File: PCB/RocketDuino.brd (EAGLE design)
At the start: 73 x 41 mm, 42 parts, among them J1 FTDI, Y1 16MHZ

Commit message: Cleanups from Reddit post
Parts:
- added C11, C12: 0.1uF, SparkFun-Capacitors:1206
- R1, R3: value 100Ω -> 150Ω
- R2, R4: value 150Ω -> 220Ω
- moved LOGO1 33.0 mm to (51.5, 37.0)
- moved SERIAL1 3.61 mm to (33.0, 4.00)
- moved RESET 2.25 mm to (18.2, 32.8)
- moved C9 2.15 mm to (16.5, 26.2), turned to 90 degrees
- moved POWER 1.00 mm to (44.8, 3.50)
- moved R1 1.00 mm to (44.8, 9.50)
- moved INFO 0.50 mm to (21.0, 6.00)
- moved R4 0.50 mm to (21.0, 11.0)
- moved GPS 0.25 mm to (24.0, 6.00)
- moved R3 0.25 mm to (24.0, 11.0)
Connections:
- net 5V: now also C11.1, C12.1
- net GND: now also C11.2, C12.2
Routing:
- net 5V: track 169.4 -> 173.2 mm, vias 2 -> 3
- net RESET: track 39.9 -> 36.7 mm
- net TX2: track 31.9 -> 35.0 mm, vias 1 -> 0
- net TX1: track 14.9 -> 17.8 mm
- net GND: track 96.5 -> 94.3 mm, vias 19 -> 21
- net RX1: track 15.7 -> 17.9 mm
- net RX2: track 34.0 -> 35.0 mm, vias 1 -> 0
- net LED_13: track 14.3 -> 13.8 mm

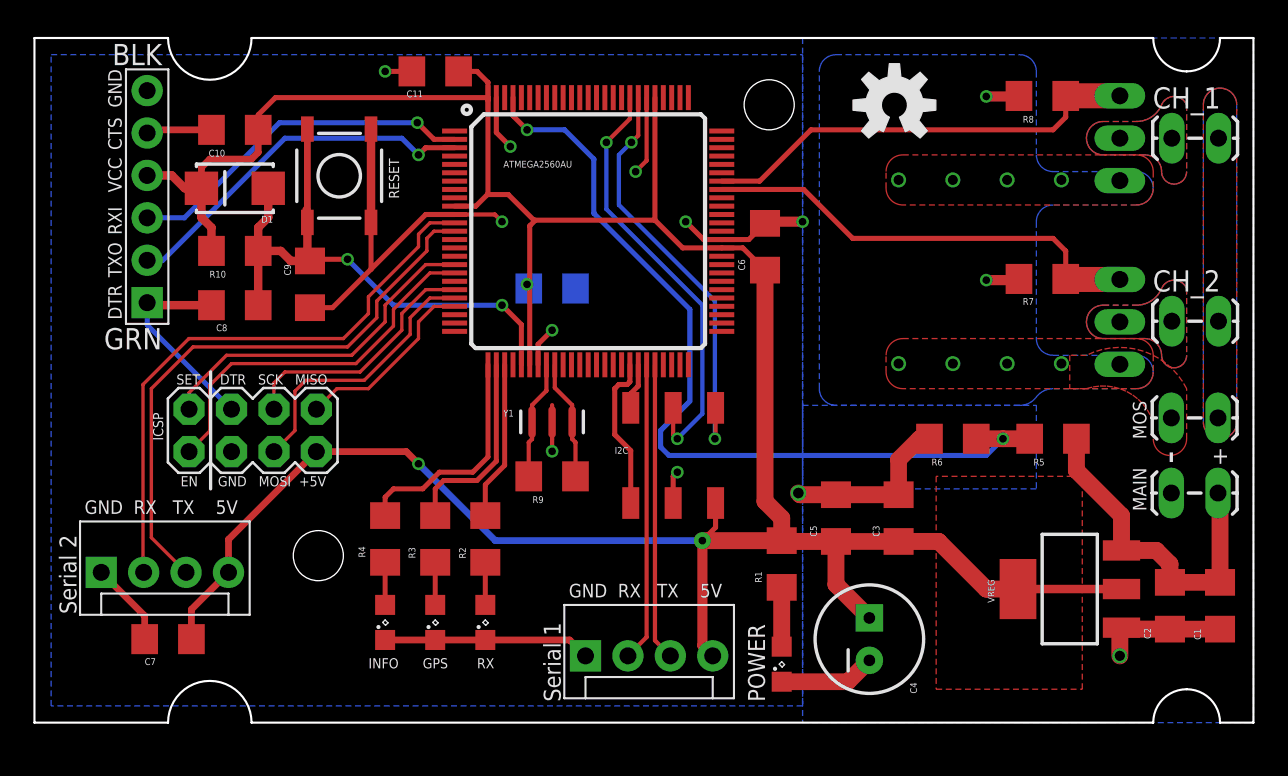
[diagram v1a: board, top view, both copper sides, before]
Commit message: Non-SMT I2C connector
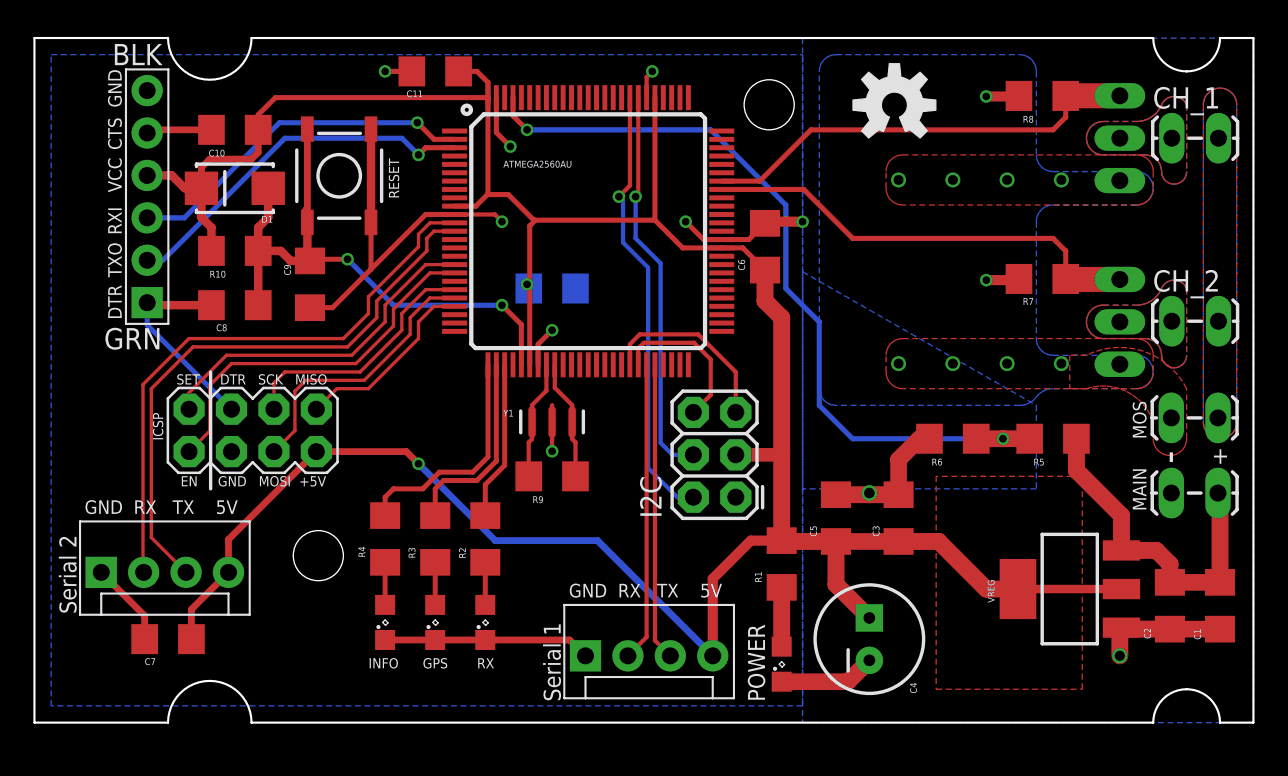
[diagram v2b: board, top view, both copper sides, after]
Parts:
- I2C: device SparkFun-Connectors:2X3_SMD -> SparkFun-Connectors:2X3
- moved I2C 4.51 mm to (42.0, 13.5), turned to 90 degrees
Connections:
- net 5V: now also I2C.3; no longer I2C.5
- net ADC14: now also I2C.2; no longer I2C.4
- net ADC15: now also I2C.4; no longer I2C.6
- net GND: now also I2C.1; no longer I2C.3
- net SCL: now also I2C.5; no longer I2C.1
- net SDA: now also I2C.6; no longer I2C.2
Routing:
- net GND: track 94.3 -> 87.2 mm, vias 21 -> 20
- net SDA: track 2.77 -> 9.48 mm
- net VSENSE: track 51.7 -> 47.5 mm
- net SCL: track 9.35 -> 11.2 mm
- net ADC15: track 25.2 -> 23.6 mm, vias 2 -> 1
- net 5V: track 173.2 -> 174.7 mm, vias 3 -> 2
- net ADC14: track 26.0 -> 26.6 mm, vias 2 -> 1

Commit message: Silkscreen Changes
Also re-routed the Vsense wire
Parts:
- moved LOGO1 51.2 mm to (4.00, 18.0)
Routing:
- net GND: track 87.2 -> 89.0 mm
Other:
- board text added: "RocketDuino"
- board text added: "V1.0"
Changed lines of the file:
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@@
 <wire x1="71" y1="41" x2="69" y2="39" width="0.127" layer="20" curve="-90"/>
 <wire x1="69" y1="39" x2="67" y2="41" width="0.127" layer="20" curve="-90"/>
-<text x="50" y="16" size="0.6096" layer="22" rot="MR0">vsense</text>
+<text x="52" y="17" size="0.6096" layer="22" rot="MR0">vsense</text>
 <text x="51.5" y="-8.25" size="1.778" layer="48">Joshua Villwock</text>
 <text x="70.5" y="15.5" size="1.016" layer="21">+</text>
@@
 <text x="1.5" y="11.25" size="1.016" layer="21" rot="R270">Serial 2</text>
 <text x="49" y="5.5" size="1.778" layer="22" rot="MR0">+</text>
+<text x="52" y="31" size="1.27" layer="21">RocketDuino</text>
+<text x="52" y="29" size="1.27" layer="21">V1.0</text>
 </plain>
 <attributes>
@@
 <element name="J1" library="SparkFun-Connectors" package="FTDI_DEVICE_SIDE" value="FTDI" x="6.75" y="31.5" locked="yes" rot="R90"/>
 <element name="D1" library="SparkFun-DiscreteSemi" package="SMA-DIODE_ALT" value="" x="12" y="32" rot="R180"/>
-<element name="LOGO1" library="SparkFun-Aesthetics" package="OSHW-LOGO-M" value="OSHW-LOGOM" x="51.5" y="36.98"/>
+<element name="LOGO1" library="SparkFun-Aesthetics" package="OSHW-LOGO-M" value="OSHW-LOGOM" x="4" y="17.98"/>
 <element name="INFO" library="led" package="SML0805" value="" x="21" y="6" smashed="yes" rot="R90">
 <attribute name="NAME" x="20" y="3.25" size="0.6096" layer="25"/>
@@
 <via x="61.5" y="32.5" extent="1-16" drill="0.6"/>
 <via x="37" y="39" extent="1-16" drill="0.4572"/>
-<via x="39" y="30" extent="1-16" drill="0.4572"/>
+<via x="38" y="31" extent="1-16" drill="0.4572"/>
 <wire x1="25.16" y1="30.43" x2="27.57" y2="30.43" width="0.254" layer="1"/>
 <wire x1="27.57" y1="30.43" x2="28" y2="30" width="0.254" layer="1"/>
@@
 <wire x1="41.16" y1="28.93" x2="42.78" y2="28.93" width="0.3048" layer="1"/>
 <wire x1="42.78" y1="28.93" x2="43.75" y2="29.9" width="0.3048" layer="1"/>
-<wire x1="41.16" y1="28.93" x2="40.07" y2="28.93" width="0.3048" layer="1"/>
-<wire x1="40.07" y1="28.93" x2="39" y2="30" width="0.3048" layer="1"/>
-<wire x1="30.16" y1="21.43" x2="30.16" y2="22.66" width="0.3" layer="1"/>
+<wire x1="41.16" y1="28.93" x2="39.32" y2="28.93" width="0.3048" layer="1"/>
 <wire x1="30.16" y1="22.66" x2="31" y2="23.5" width="0.3" layer="1"/>
 <via x="65" y="4" extent="1-16" drill="0.6096"/>
@@
 <wire x1="57" y1="26.5" x2="58.96" y2="26.5" width="0.6096" layer="1"/>
 <polygon width="0.254" layer="16" isolate="0.5" orphans="yes">
-<vertex x="46" y="27"/>
+<vertex x="46" y="39"/>
 <vertex x="60" y="19"/>
 <vertex x="60" y="14"/>
@@
 <wire x1="36.66" y1="38.66" x2="37" y2="39" width="0.254" layer="1"/>
 <contactref element="I2C" pad="1"/>
+<wire x1="30.16" y1="21.43" x2="30.16" y2="22.66" width="0.3" layer="1"/>
+<wire x1="39.32" y1="28.93" x2="38" y2="30.25" width="0.3048" layer="1"/>
+<wire x1="38" y1="30.25" x2="38" y2="31" width="0.3048" layer="1"/>
 </signal>
 <signal name="RESET">
@@
 <via x="58" y="17" extent="1-16" drill="0.4572"/>
 <wire x1="49" y1="17" x2="58" y2="17" width="0.3048" layer="16"/>
-<wire x1="47" y1="24" x2="47" y2="19" width="0.3048" layer="16"/>
-<wire x1="47" y1="19" x2="49" y2="17" width="0.3048" layer="16"/>
-<wire x1="29.5" y1="35.5" x2="40.5" y2="35.5" width="0.3048" layer="16"/>
-<wire x1="40.5" y1="35.5" x2="45" y2="31" width="0.3048" layer="16"/>
-<wire x1="45" y1="31" x2="45" y2="26" width="0.3048" layer="16"/>
-<wire x1="45" y1="26" x2="47" y2="24" width="0.3048" layer="16"/>
+<wire x1="44" y1="20" x2="46" y2="20" width="0.3048" layer="16"/>
+<wire x1="46" y1="20" x2="49" y2="17" width="0.3048" layer="16"/>
+<wire x1="39.5" y1="34" x2="39.5" y2="24.5" width="0.3048" layer="16"/>
+<wire x1="39.5" y1="24.5" x2="44" y2="20" width="0.3048" layer="16"/>
+<wire x1="29.5" y1="35.5" x2="38" y2="35.5" width="0.3048" layer="16"/>
+<wire x1="38" y1="35.5" x2="39.5" y2="34" width="0.3048" layer="16"/>
 </signal>
 <signal name="SCK">

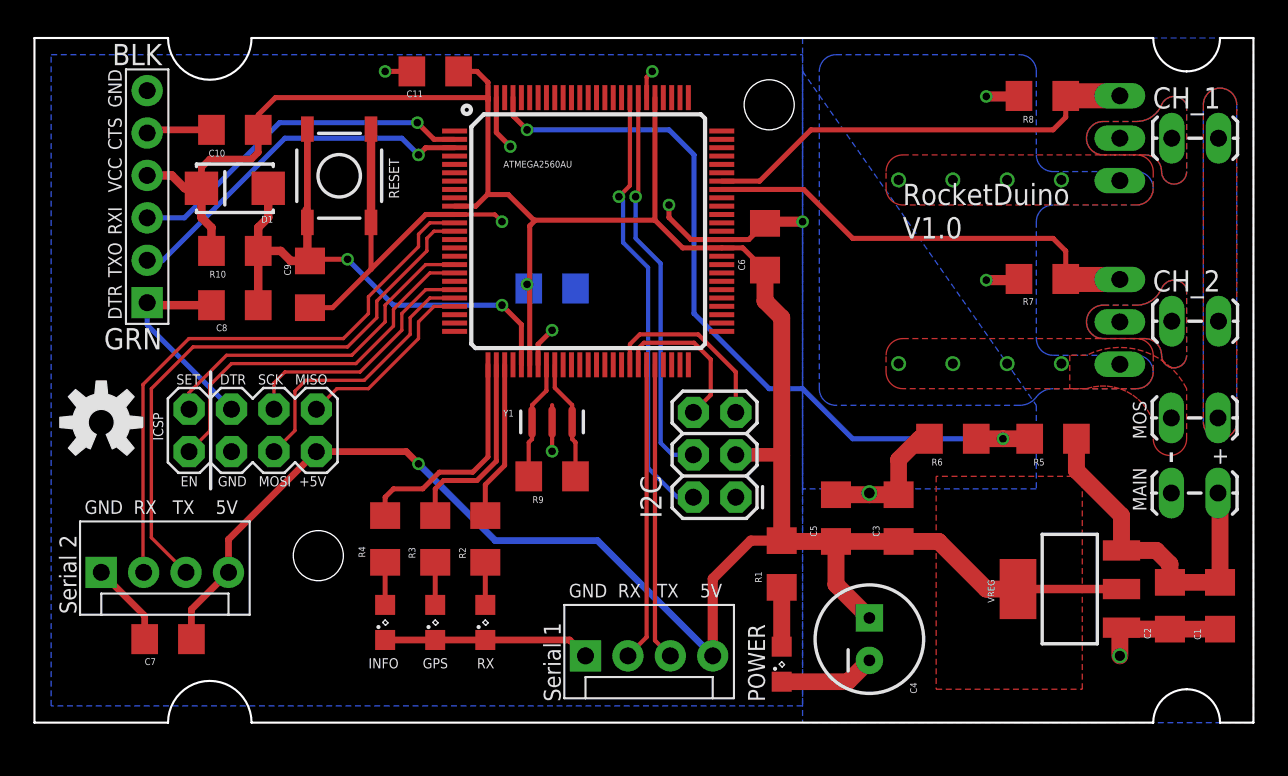
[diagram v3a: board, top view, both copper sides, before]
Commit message: Minor Re-routes of traces
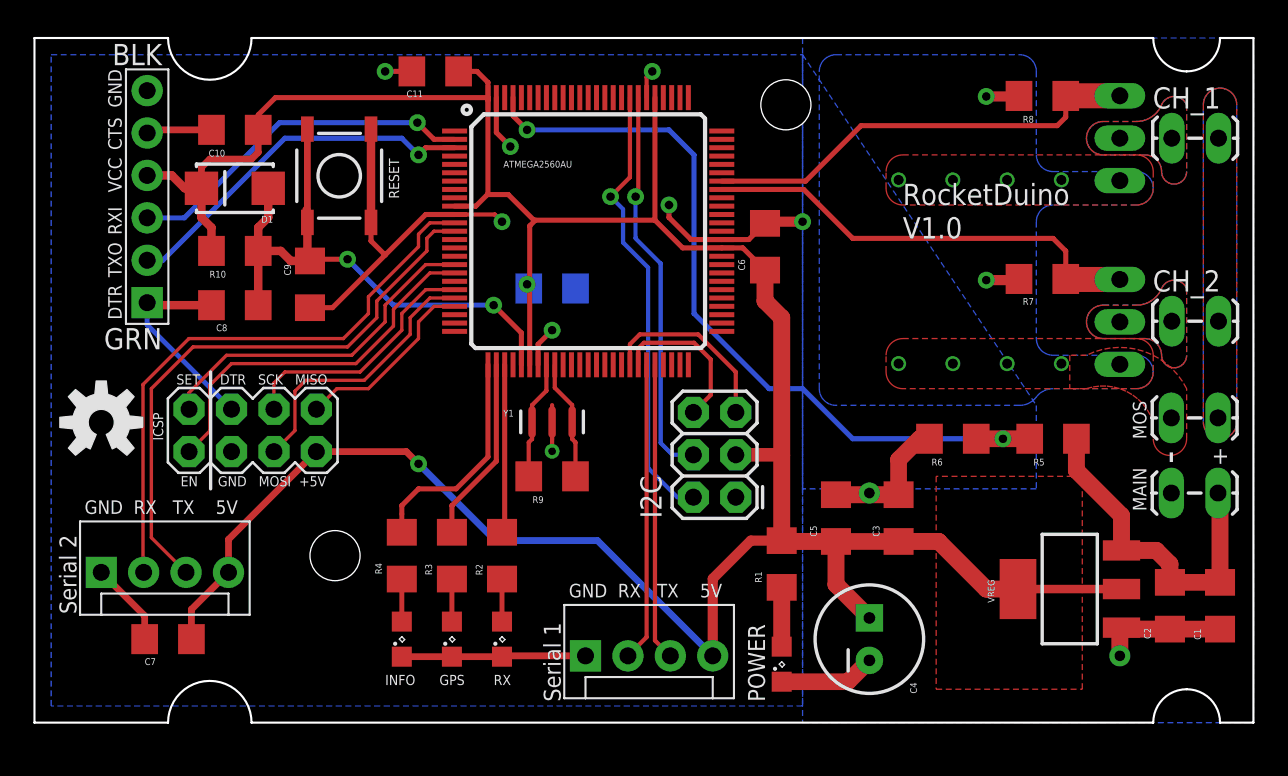
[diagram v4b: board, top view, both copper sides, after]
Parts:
- moved GPS 1.41 mm to (25.0, 5.00)
- moved INFO 1.41 mm to (22.0, 5.00)
- moved R2 1.41 mm to (28.0, 10.0)
- moved R3 1.41 mm to (25.0, 10.0)
- moved R4 1.41 mm to (22.0, 10.0)
- moved RX 1.41 mm to (28.0, 5.00)
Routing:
- net GND: track 89.0 -> 87.2 mm
- net LED_RX: track 9.51 -> 10.1 mm
- net LED_GPS: track 11.7 -> 11.1 mm

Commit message: Silkscreen changes
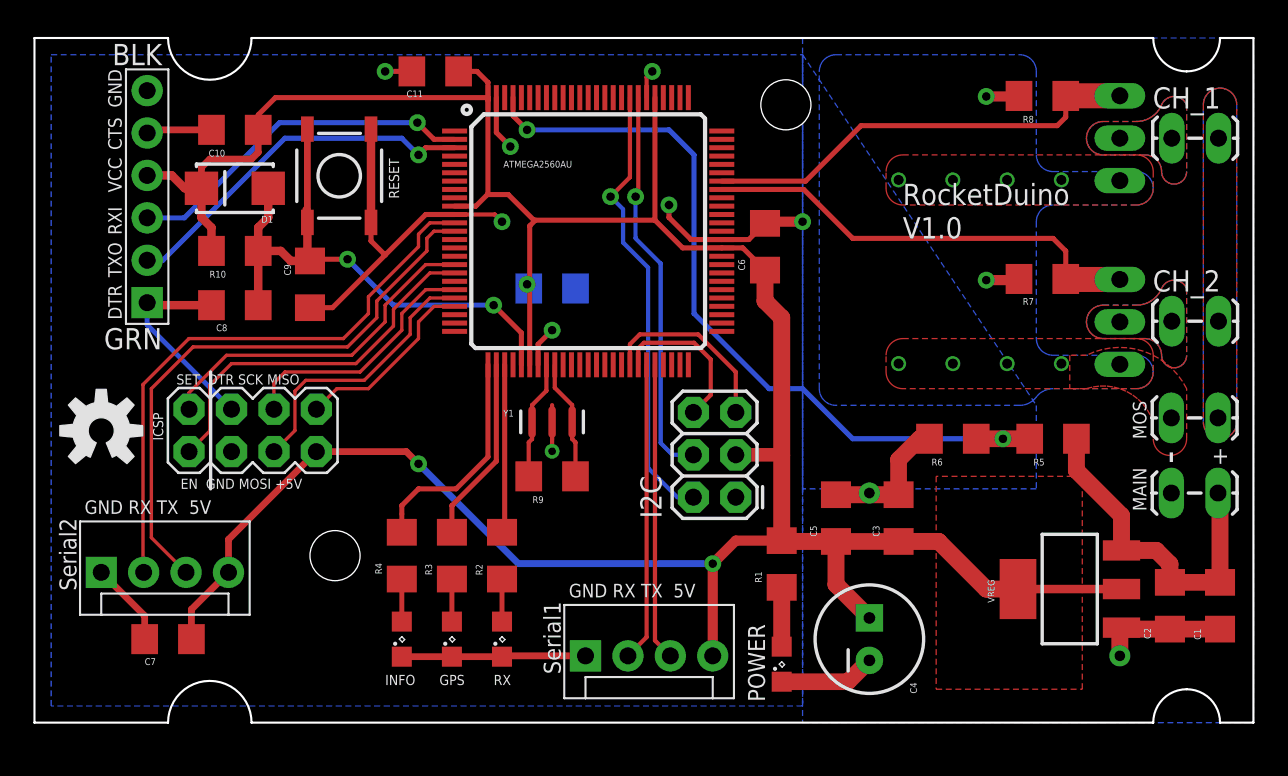
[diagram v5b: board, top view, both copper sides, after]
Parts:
- added LOGO2: OSHW-LOGOM, SparkFun-Aesthetics:OSHW-LOGO-M
- moved LOGO1 0.50 mm to (4.00, 17.5)
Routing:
- net 5V: track 174.7 -> 173.0 mm, vias 2 -> 3
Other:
- board text added: "Serial1"
- board text added: "Serial2"
- board text removed: "Serial 1"
- board text removed: "Serial 2"
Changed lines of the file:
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@@
 <setting verticaltext="up"/>
 </settings>
-<grid distance="39.3700787" unitdist="mil" unit="mil" style="lines" multiple="1" display="yes" altdistance="0.25" altunitdist="mm" altunit="mm"/>
+<grid distance="0.999999999" unitdist="mm" unit="mm" style="lines" multiple="1" display="yes" altdistance="0.25" altunitdist="mm" altunit="mm"/>
 <layers>
 <layer number="1" name="Top" color="4" fill="1" visible="yes" active="yes"/>
@@
 <wire x1="71" y1="41" x2="69" y2="39" width="0.127" layer="20" curve="-90"/>
 <wire x1="69" y1="39" x2="67" y2="41" width="0.127" layer="20" curve="-90"/>
-<text x="52" y="17" size="0.6096" layer="22" rot="MR0">vsense</text>
+<text x="37" y="35.75" size="0.6096" layer="22" rot="MR0">vsense</text>
 <text x="51.5" y="-8.25" size="1.778" layer="48">Joshua Villwock</text>
 <text x="70.5" y="15.5" size="1.016" layer="21">+</text>
@@
 <hole x="45" y="37" drill="3"/>
 <hole x="18" y="10" drill="3"/>
-<text x="8.5" y="20.25" size="0.6096" layer="21">SET     DTR   SCK   MISO</text>
-<text x="8.75" y="14.15" size="0.6096" layer="21">EN     GND   MOSI  +5V</text>
+<text x="8.5" y="20.25" size="0.6096" layer="21" font="vector" ratio="18">SET  DTR SCK MISO</text>
 <wire x1="10.55" y1="21" x2="10.55" y2="14" width="0.2" layer="21"/>
 <wire x1="69" y1="2" x2="71" y2="0" width="0.127" layer="20" curve="-90"/>
 <wire x1="67" y1="0" x2="69" y2="2" width="0.127" layer="20" curve="-90"/>
-<text x="32" y="7.5" size="0.8128" layer="21">GND  RX   TX    5V</text>
-<text x="3" y="12.5" size="0.8128" layer="21">GND  RX   TX    5V</text>
-<text x="30.5" y="6" size="1.016" layer="21" rot="R270">Serial 1</text>
-<text x="1.5" y="11.25" size="1.016" layer="21" rot="R270">Serial 2</text>
+<text x="30.5" y="7.25" size="1.016" layer="21" rot="R270">Serial1</text>
+<text x="1.5" y="12.25" size="1.016" layer="21" ratio="10" rot="R270">Serial2</text>
 <text x="49" y="5.5" size="1.778" layer="22" rot="MR0">+</text>
-<text x="52" y="31" size="1.27" layer="21">RocketDuino</text>
-<text x="52" y="29" size="1.27" layer="21">V1.0</text>
+<text x="52" y="31" size="1.27" layer="21" font="vector" ratio="9">RocketDuino</text>
+<text x="52" y="29" size="1.27" layer="21" font="vector" ratio="9">V1.0</text>
+<text x="3" y="12.5" size="0.8128" layer="21" font="vector" ratio="19">GND RX TX  5V</text>
+<text x="8.75" y="14" size="0.6096" layer="21" font="vector" ratio="18">EN  GND MOSI +5V</text>
+<text x="32" y="7.5" size="0.8128" layer="21" font="vector" ratio="19">GND RX TX  5V</text>
 </plain>
 <attributes>
@@
 </class>
 </classes>
-<designrules name="Smart Prototyping">
+<designrules name="MakerStudio">
 <description language="de">&lt;b&gt;EAGLE Design Rules&lt;/b&gt;
 &lt;p&gt;
@@
 necessary adjustments and save your customized
 design rules under a new name.</description>
-<description language="zh">&lt;b&gt;NOA-Labs EAGLE Design Rules&lt;/b&gt;
+<description language="zh">&lt;b&gt;Seeed Studio EAGLE Design Rules&lt;/b&gt;
 </description>
 <param name="layerSetup" value="(1*16)"/>
@@
 <param name="mdViaViaSameLayer" value="8mil"/>
 <param name="mnLayersViaInSmd" value="2"/>
-<param name="mdCopperDimension" value="0.4mm"/>
+<param name="mdCopperDimension" value="10mil"/>
 <param name="mdDrill" value="10mil"/>
 <param name="mdSmdStop" value="0mil"/>
 <param name="msWidth" value="6mil"/>
-<param name="msDrill" value="0.3mm"/>
+<param name="msDrill" value="12mil"/>
 <param name="msMicroVia" value="12mil"/>
 <param name="msBlindViaRatio" value="0.5"/>
@@
 <param name="mlMinCreamFrame" value="0mil"/>
 <param name="mlMaxCreamFrame" value="0mil"/>
-<param name="mlViaStopLimit" value="25mil"/>
+<param name="mlViaStopLimit" value="100mil"/>
 <param name="srRoundness" value="0"/>
 <param name="srMinRoundness" value="0mil"/>
@@
 <element name="J1" library="SparkFun-Connectors" package="FTDI_DEVICE_SIDE" value="FTDI" x="6.75" y="31.5" locked="yes" rot="R90"/>
 <element name="D1" library="SparkFun-DiscreteSemi" package="SMA-DIODE_ALT" value="" x="12" y="32" rot="R180"/>
-<element name="LOGO1" library="SparkFun-Aesthetics" package="OSHW-LOGO-M" value="OSHW-LOGOM" x="4" y="17.98"/>
+<element name="LOGO1" library="SparkFun-Aesthetics" package="OSHW-LOGO-M" value="OSHW-LOGOM" x="4" y="17.48"/>
 <element name="INFO" library="led" package="SML0805" value="" x="22" y="5" smashed="yes" rot="R90">
 <attribute name="NAME" x="21" y="2.25" size="0.6096" layer="25"/>
@@
 </element>
 <element name="C12" library="SparkFun-Capacitors" package="1206" value="0.1uF" x="31" y="26" rot="MR180"/>
+<element name="LOGO2" library="SparkFun-Aesthetics" package="OSHW-LOGO-M" value="OSHW-LOGOM" x="4" y="17.5" rot="MR0"/>
 </elements>
 <signals>
@@
 <via x="23" y="15.5" extent="1-16" drill="0.508" diameter="1.016"/>
 <contactref element="SERIAL1" pad="4"/>
-<wire x1="23" y1="15.5" x2="27.6" y2="10.9" width="0.4064" layer="16"/>
 <contactref element="SERIAL2" pad="4"/>
 <wire x1="16.88" y1="16.23" x2="11.62" y2="10.97" width="0.4064" layer="1"/>
@@
 <wire x1="42" y1="16.04" x2="44.75" y2="16.04" width="0.8128" layer="1"/>
 <wire x1="44.75" y1="16.04" x2="44.75" y2="16" width="0.8128" layer="1"/>
-<wire x1="40.62" y1="4" x2="40.62" y2="8.62" width="0.6096" layer="1"/>
-<wire x1="40.62" y1="8.62" x2="42.9" y2="10.9" width="0.6096" layer="1"/>
-<wire x1="42.9" y1="10.9" x2="44.75" y2="10.9" width="0.6096" layer="1"/>
-<wire x1="27.6" y1="10.9" x2="33.72" y2="10.9" width="0.4064" layer="16"/>
-<wire x1="33.72" y1="10.9" x2="40.62" y2="4" width="0.4064" layer="16"/>
+<wire x1="42" y1="10.9" x2="44.75" y2="10.9" width="0.6096" layer="1"/>
+<wire x1="40.62" y1="4" x2="40.62" y2="9.52" width="0.6096" layer="1"/>
+<wire x1="23" y1="15.5" x2="28.98" y2="9.52" width="0.4064" layer="16"/>
+<via x="40.62" y="9.52" extent="1-16" drill="0.508" diameter="1.016"/>
+<wire x1="40.62" y1="9.52" x2="28.98" y2="9.52" width="0.4064" layer="16"/>
+<wire x1="42" y1="10.9" x2="40.62" y2="9.52" width="0.6096" layer="1"/>
 </signal>
 <signal name="TX1">
